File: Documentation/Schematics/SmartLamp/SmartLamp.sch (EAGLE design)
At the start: 31 parts, among them J2 AVR_SPI_PROG_5X2PTH2, Q1 STN4NF03L, Q2 STN4NF03L, Q3 STN4NF03L, U1 MIC2920A, U2 DS3231MZ, U3 ATMEGA8/168/328, U4 HM-10

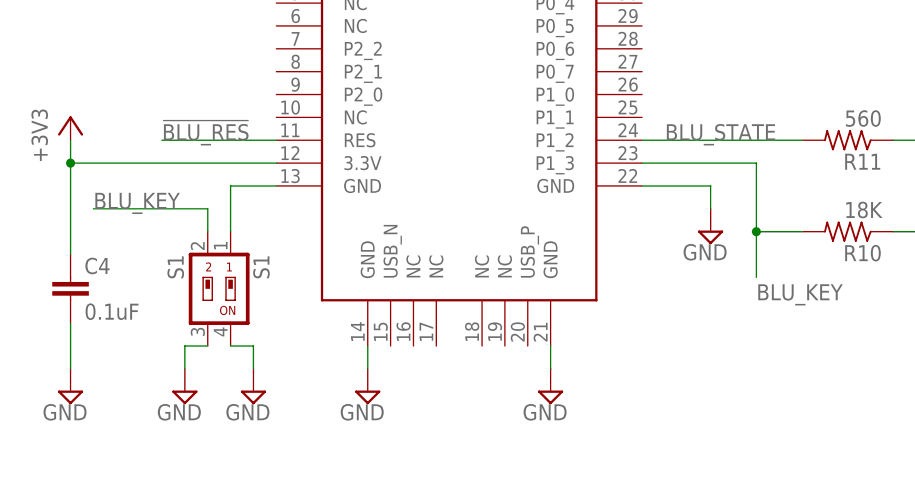
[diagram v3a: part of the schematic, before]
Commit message: Fixed GND - switch connection for HM-10
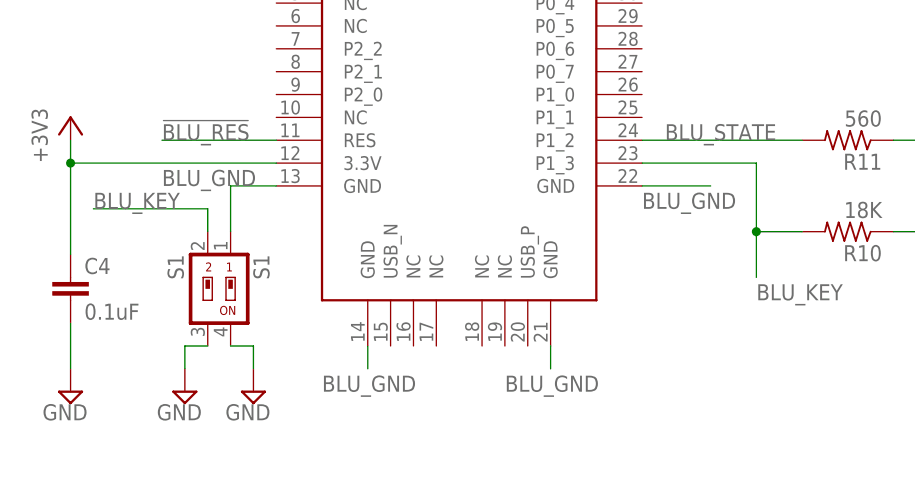
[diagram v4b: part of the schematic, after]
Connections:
- removed net BLU_SWITCH: S1.1, U4.GND@1
- new net BLU_GND: S1.1, U4.GND@1, U4.GND@2, U4.GND@3, U4.GND@4
- net GND: no longer U4.GND@2, U4.GND@3, U4.GND@4
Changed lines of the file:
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@@
 <grid distance="0.1" unitdist="inch" unit="inch" style="lines" multiple="1" display="no" altdistance="0.01" altunitdist="inch" altunit="inch"/>
 <layers>
-<layer number="1" name="Top" color="4" fill="1" visible="yes" active="no"/>
-<layer number="16" name="Bottom" color="1" fill="1" visible="yes" active="no"/>
-<layer number="17" name="Pads" color="2" fill="1" visible="yes" active="no"/>
-<layer number="18" name="Vias" color="2" fill="1" visible="yes" active="no"/>
-<layer number="19" name="Unrouted" color="6" fill="1" visible="yes" active="no"/>
-<layer number="20" name="Dimension" color="15" fill="1" visible="yes" active="no"/>
-<layer number="21" name="tPlace" color="7" fill="1" visible="yes" active="no"/>
-<layer number="22" name="bPlace" color="7" fill="1" visible="yes" active="no"/>
-<layer number="23" name="tOrigins" color="15" fill="1" visible="yes" active="no"/>
-<layer number="24" name="bOrigins" color="15" fill="1" visible="yes" active="no"/>
-<layer number="25" name="tNames" color="7" fill="1" visible="yes" active="no"/>
-<layer number="26" name="bNames" color="7" fill="1" visible="yes" active="no"/>
-<layer number="27" name="tValues" color="7" fill="1" visible="yes" active="no"/>
-<layer number="28" name="bValues" color="7" fill="1" visible="yes" active="no"/>
+<layer number="1" name="Top" color="4" fill="1" visible="no" active="no"/>
+<layer number="16" name="Bottom" color="1" fill="1" visible="no" active="no"/>
+<layer number="17" name="Pads" color="2" fill="1" visible="no" active="no"/>
+<layer number="18" name="Vias" color="2" fill="1" visible="no" active="no"/>
+<layer number="19" name="Unrouted" color="6" fill="1" visible="no" active="no"/>
+<layer number="20" name="Dimension" color="15" fill="1" visible="no" active="no"/>
+<layer number="21" name="tPlace" color="7" fill="1" visible="no" active="no"/>
+<layer number="22" name="bPlace" color="7" fill="1" visible="no" active="no"/>
+<layer number="23" name="tOrigins" color="15" fill="1" visible="no" active="no"/>
+<layer number="24" name="bOrigins" color="15" fill="1" visible="no" active="no"/>
+<layer number="25" name="tNames" color="7" fill="1" visible="no" active="no"/>
+<layer number="26" name="bNames" color="7" fill="1" visible="no" active="no"/>
+<layer number="27" name="tValues" color="7" fill="1" visible="no" active="no"/>
+<layer number="28" name="bValues" color="7" fill="1" visible="no" active="no"/>
 <layer number="29" name="tStop" color="7" fill="3" visible="no" active="no"/>
 <layer number="30" name="bStop" color="7" fill="6" visible="no" active="no"/>
@@
 <layer number="35" name="tGlue" color="7" fill="4" visible="no" active="no"/>
 <layer number="36" name="bGlue" color="7" fill="5" visible="no" active="no"/>
-<layer number="37" name="tTest" color="7" fill="1" visible="yes" active="no"/>
-<layer number="38" name="bTest" color="7" fill="1" visible="yes" active="no"/>
+<layer number="37" name="tTest" color="7" fill="1" visible="no" active="no"/>
+<layer number="38" name="bTest" color="7" fill="1" visible="no" active="no"/>
 <layer number="39" name="tKeepout" color="4" fill="11" visible="no" active="no"/>
 <layer number="40" name="bKeepout" color="1" fill="11" visible="no" active="no"/>
@@
 <layer number="44" name="Drills" color="7" fill="1" visible="no" active="no"/>
 <layer number="45" name="Holes" color="7" fill="1" visible="no" active="no"/>
-<layer number="46" name="Milling" color="3" fill="1" visible="yes" active="no"/>
-<layer number="47" name="Measures" color="7" fill="1" visible="yes" active="no"/>
-<layer number="48" name="Document" color="7" fill="1" visible="yes" active="no"/>
-<layer number="49" name="Reference" color="7" fill="1" visible="yes" active="no"/>
-<layer number="50" name="dxf" color="7" fill="1" visible="yes" active="no"/>
-<layer number="51" name="tDocu" color="7" fill="1" visible="yes" active="no"/>
-<layer number="52" name="bDocu" color="7" fill="1" visible="yes" active="no"/>
-<layer number="53" name="tGND_GNDA" color="7" fill="9" visible="yes" active="no"/>
-<layer number="54" name="bGND_GNDA" color="1" fill="9" visible="yes" active="no"/>
-<layer number="56" name="wert" color="7" fill="1" visible="yes" active="no"/>
-<layer number="57" name="tCAD" color="7" fill="1" visible="yes" active="no"/>
-<layer number="59" name="tCarbon" color="7" fill="1" visible="yes" active="no"/>
-<layer number="60" name="bCarbon" color="7" fill="1" visible="yes" active="no"/>
+<layer number="46" name="Milling" color="3" fill="1" visible="no" active="no"/>
+<layer number="47" name="Measures" color="7" fill="1" visible="no" active="no"/>
+<layer number="48" name="Document" color="7" fill="1" visible="no" active="no"/>
+<layer number="49" name="Reference" color="7" fill="1" visible="no" active="no"/>
+<layer number="50" name="dxf" color="7" fill="1" visible="no" active="no"/>
+<layer number="51" name="tDocu" color="7" fill="1" visible="no" active="no"/>
+<layer number="52" name="bDocu" color="7" fill="1" visible="no" active="no"/>
+<layer number="53" name="tGND_GNDA" color="7" fill="9" visible="no" active="no"/>
+<layer number="54" name="bGND_GNDA" color="1" fill="9" visible="no" active="no"/>
+<layer number="56" name="wert" color="7" fill="1" visible="no" active="no"/>
+<layer number="57" name="tCAD" color="7" fill="1" visible="no" active="no"/>
+<layer number="59" name="tCarbon" color="7" fill="1" visible="no" active="no"/>
+<layer number="60" name="bCarbon" color="7" fill="1" visible="no" active="no"/>
 <layer number="90" name="Modules" color="5" fill="1" visible="yes" active="yes"/>
 <layer number="91" name="Nets" color="2" fill="1" visible="yes" active="yes"/>
@@
 <part name="BLU_STATE" library="adafruit" deviceset="LED" device="CHIPLED_1206" value="BLUE"/>
 <part name="GND7" library="supply2" deviceset="GND" device=""/>
-<part name="GND8" library="supply2" deviceset="GND" device=""/>
-<part name="GND9" library="supply2" deviceset="GND" device=""/>
-<part name="GND11" library="supply2" deviceset="GND" device=""/>
 <part name="GND1" library="supply2" deviceset="GND" device=""/>
 <part name="C4" library="rcl" deviceset="C-EU" device="C1206" value="0.1uF"/>
@@
 </instance>
 <instance part="GND7" gate="GND" x="119.38" y="15.24" rot="MR0"/>
-<instance part="GND8" gate="GND" x="132.08" y="15.24" rot="MR0"/>
-<instance part="GND9" gate="GND" x="152.4" y="15.24" rot="MR0"/>
-<instance part="GND11" gate="GND" x="170.18" y="33.02" rot="MR0"/>
 <instance part="GND1" gate="GND" x="203.2" y="40.64" rot="MR0"/>
 <instance part="C4" gate="G$1" x="99.06" y="27.94"/>
@@
 </segment>
 <segment>
-<pinref part="U4" gate="G$1" pin="GND@2"/>
-<wire x1="132.08" y1="20.32" x2="132.08" y2="17.78" width="0.1524" layer="91"/>
-<pinref part="GND8" gate="GND" pin="GND"/>
-</segment>
-<segment>
-<pinref part="U4" gate="G$1" pin="GND@3"/>
-<wire x1="152.4" y1="20.32" x2="152.4" y2="17.78" width="0.1524" layer="91"/>
-<pinref part="GND9" gate="GND" pin="GND"/>
-</segment>
-<segment>
-<pinref part="U4" gate="G$1" pin="GND@4"/>
-<wire x1="162.56" y1="38.1" x2="170.18" y2="38.1" width="0.1524" layer="91"/>
-<wire x1="170.18" y1="38.1" x2="170.18" y2="35.56" width="0.1524" layer="91"/>
-<pinref part="GND11" gate="GND" pin="GND"/>
-</segment>
-<segment>
 <pinref part="BLU_STATE" gate="G$1" pin="C"/>
 <wire x1="200.66" y1="43.18" x2="203.2" y2="43.18" width="0.1524" layer="91"/>
@@
 </segment>
 </net>
-<net name="BLU_SWITCH" class="0">
-<segment>
-<pinref part="U4" gate="G$1" pin="GND@1"/>
-<wire x1="116.84" y1="38.1" x2="121.92" y2="38.1" width="0.1524" layer="91"/>
-<pinref part="S1" gate="G$1" pin="1"/>
-<wire x1="116.84" y1="38.1" x2="116.84" y2="33.02" width="0.1524" layer="91"/>
-</segment>
-</net>
 <net name="MISO" class="0">
 <segment>
@@
 </segment>
 </net>
+<net name="BLU_GND" class="1">
+<segment>
+<pinref part="U4" gate="G$1" pin="GND@2"/>
+<wire x1="132.08" y1="20.32" x2="132.08" y2="17.78" width="0.1524" layer="91"/>
+<label x="127" y="15.24" size="1.778" layer="95" font="vector"/>
+</segment>
+<segment>
+<pinref part="S1" gate="G$1" pin="1"/>
+<wire x1="116.84" y1="38.1" x2="116.84" y2="33.02" width="0.1524" layer="91"/>
+<pinref part="U4" gate="G$1" pin="GND@1"/>
+<wire x1="121.92" y1="38.1" x2="116.84" y2="38.1" width="0.1524" layer="91"/>
+<label x="109.22" y="38.1" size="1.778" layer="95" font="vector"/>
+</segment>
+<segment>
+<pinref part="U4" gate="G$1" pin="GND@4"/>
+<wire x1="162.56" y1="38.1" x2="170.18" y2="38.1" width="0.1524" layer="91"/>
+<label x="162.56" y="35.56" size="1.778" layer="95" font="vector"/>
+</segment>
+<segment>
+<pinref part="U4" gate="G$1" pin="GND@3"/>
+<wire x1="152.4" y1="20.32" x2="152.4" y2="17.78" width="0.1524" layer="91"/>
+<label x="147.32" y="15.24" size="1.778" layer="95" font="vector"/>
+</segment>
+</net>

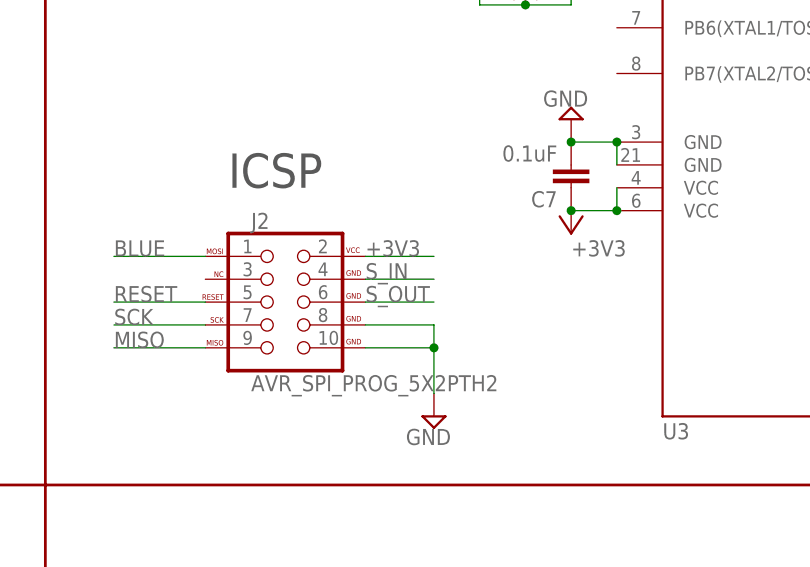
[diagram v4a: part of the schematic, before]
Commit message: Fixed TX and RX swapped on PCB...
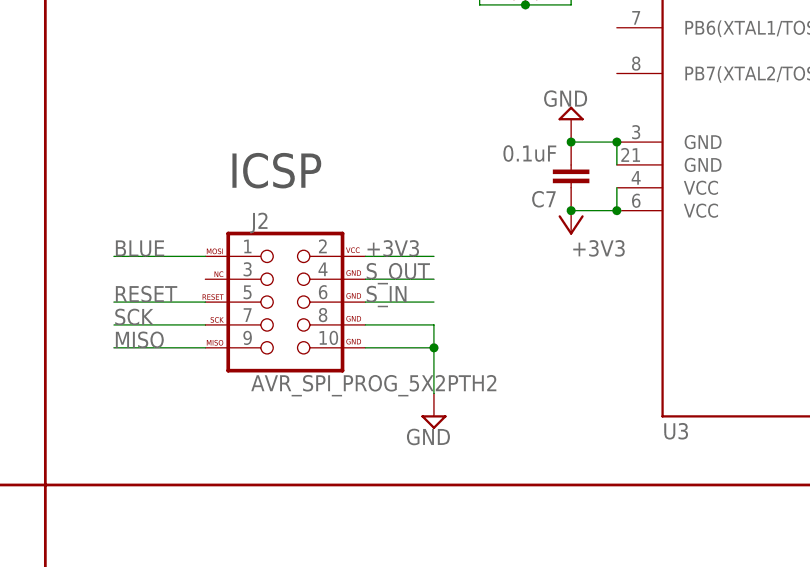
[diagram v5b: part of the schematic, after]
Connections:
- net S_IN: now also J2.GND@2; no longer J2.GND@1
- net S_OUT: now also J2.GND@1; no longer J2.GND@2
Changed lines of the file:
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@@
 </segment>
 <segment>
-<pinref part="J2" gate="G$1" pin="GND@2"/>
-<wire x1="248.92" y1="106.68" x2="256.54" y2="106.68" width="0.1524" layer="91"/>
-<label x="248.92" y="106.68" size="1.778" layer="95" font="vector"/>
+<pinref part="J2" gate="G$1" pin="GND@1"/>
+<wire x1="248.92" y1="109.22" x2="256.54" y2="109.22" width="0.1524" layer="91"/>
+<label x="248.92" y="109.22" size="1.778" layer="95" font="vector"/>
 </segment>
 </net>
@@
 </segment>
 <segment>
-<pinref part="J2" gate="G$1" pin="GND@1"/>
-<wire x1="248.92" y1="109.22" x2="256.54" y2="109.22" width="0.1524" layer="91"/>
-<label x="248.92" y="109.22" size="1.778" layer="95" font="vector"/>
+<pinref part="J2" gate="G$1" pin="GND@2"/>
+<wire x1="248.92" y1="106.68" x2="256.54" y2="106.68" width="0.1524" layer="91"/>
+<label x="248.92" y="106.68" size="1.778" layer="95" font="vector"/>
 </segment>
 </net>
